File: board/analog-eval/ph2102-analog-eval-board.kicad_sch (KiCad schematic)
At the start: 41 parts, among them J1 CONN_PROBE, U1 LMC662, U2 TLV2333, U3 REF3020, U4 MCP3201-BI/SN, U5 LM27762

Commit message: 板子修改
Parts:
- removed U?: ESP32-PICO-D4, Package_DFN_QFN:QFN-48-1EP_7x7mm_P0.5mm_EP5.3x5.3mm, symbol RF_Module:ESP32-PICO-D4
- added R18: 0R0, Resistor_SMD:R_0805_2012Metric, symbol Device:R_Small
- R7: footprint (none) -> Resistor_SMD:R_0402_1005Metric
- U1: footprint (none) -> Package_SO:SOIC-8_3.9x4.9mm_P1.27mm
- gave numbers to parts that had none: 8
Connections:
- net at R10.1, R9.1, U1.3 (+): now also R18.1; no longer U1.6 (-)
- new net: R18.2, U1.6 (-)
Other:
- title: (none) -> PH 计模拟前端验证版
- moved on the sheet: C14, C15, C16, R13, R14, R15, R16, R17, U5

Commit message: update
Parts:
- removed NT1: NetTie_3_Tee, symbol Device:NetTie_3_Tee
- added C17: 10u, Capacitor_SMD:C_0603_1608Metric, symbol Device:C_Small
- added C18, C19: 2u2, Capacitor_SMD:C_0603_1608Metric, symbol Device:C_Small
- added C20, C21: 100n, Capacitor_SMD:C_0603_1608Metric, symbol Device:C_Small
- added C22: 100u, Capacitor_Tantalum_SMD:CP_EIA-3528-15_AVX-H, symbol Device:C_Polarized_Small
- added H1, H2, H3, H4: M3, MountingHole:MountingHole_3.2mm_M3_Pad_Via, symbol Mechanical:MountingHole_Pad
- added J2: CONN_OUT, Connector_PinHeader_2.54mm:PinHeader_1x10_P2.54mm_Vertical, symbol Connector_Generic:Conn_01x10
- added J3: CONN_NTC, Connector_JST:JST_XH_S2B-XH-A-1_1x02_P2.50mm_Horizontal, symbol Connector_Generic:Conn_01x02
- added NT1: NetTie_2, NetTie:NetTie-2_SMD_Pad2.0mm, symbol Device:NetTie_2
- added R19: 10k/1%, Resistor_SMD:R_0603_1608Metric, symbol Device:R_Small
- added R21, R22: 100R, Resistor_SMD:R_0603_1608Metric, symbol Device:R_Small
- added R23: 10k, Resistor_SMD:R_0603_1608Metric, symbol Device:R_Small
- added TP1: TP_PGOOD, TestPoint:TestPoint_Pad_D1.0mm, symbol Connector:TestPoint
- added TP2: TP_GUARD, symbol Connector:TestPoint
- added TP3: TP_+2V5, TestPoint:TestPoint_Pad_D1.0mm, symbol Connector:TestPoint
- added TP4: TP_-2V5, TestPoint:TestPoint_Pad_D1.0mm, symbol Connector:TestPoint
- C1, C10, C11, C12, C13, C14, C15, C2, C3, C4, C5, C6, C8, C9: footprint (none) -> Capacitor_SMD:C_0603_1608Metric
- C16: value 1u -> 4u7; footprint (none) -> Capacitor_SMD:C_0603_1608Metric
- C7: value 100n -> 1n; footprint (none) -> Capacitor_SMD:C_0603_1608Metric
- J1: footprint (none) -> Connector_Coaxial:BNC_Amphenol_B6252HB-NPP3G-50_Horizontal
- R1, R2, R3, R4: value 100k -> 10k/1%; footprint (none) -> Resistor_SMD:R_0603_1608Metric
- R10: value 91k -> 9.1k/1%; footprint (none) -> Resistor_SMD:R_0603_1608Metric
- R11, R12, R14, R15, R16, R17, R5, R6, R8: footprint (none) -> Resistor_SMD:R_0603_1608Metric
- R13: value R_Small -> 10k; footprint (none) -> Resistor_SMD:R_0603_1608Metric
- R18: footprint Resistor_SMD:R_0805_2012Metric -> Resistor_SMD:R_1206_3216Metric_Pad1.30x1.75mm_HandSolder
- R7: footprint Resistor_SMD:R_0402_1005Metric -> Resistor_SMD:R_0603_1608Metric
- R9: value 91k -> 10k/1%; footprint (none) -> Resistor_SMD:R_0603_1608Metric
- U2, U4: footprint (none) -> Package_SO:SOIC-8_3.9x4.9mm_P1.27mm
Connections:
- net +3V0 is gone; now on net +2V5: C4.2, C5.2, U3.1 (IN)
- net +2V5: now also R14.1, U5.11 (OUT+), C18.1, TP3.1
- net +3V3: now also U5.12 (EN+), U5.8 (EN-), C17.2, C22.1, J2.1 (Pin_1); no longer R13.2
- net -2V5: now also R15.2, U5.6 (OUT-), C19.2, TP4.1
- net ADC_CS: now also J2.3 (Pin_3)
- net ADC_MISO: now also J2.4 (Pin_4)
- net ADC_SCK: now also J2.5 (Pin_5)
- net GNDA: now also R16.2, R17.2, C17.1, C18.2, C19.1, C20.2, C21.2, C22.2, H1.1, H2.1, H3.1, H4.1, J2.10 (Pin_10), J2.6 (Pin_6), J3.2 (Pin_2), NT1.1
- net GUARD: now also TP2.1
- net VREF: now also J2.7 (Pin_7), R19.2
- net at C6.2, R12.2, R6.2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: now also R22.1; no longer C7.2, U4.2 (IN+)
- net at R13.1: now also TP1.1; no longer U5.1 (PGOOD)
- net at U2.5 (+): now also C21.1, R23.2
- net at U2.6 (-): now also U2.7, R21.1
- new net: R13.2, U5.1 (PGOOD)
- new net GND: J2.2 (Pin_2), NT1.2
- new net NTC_IN: J3.1 (Pin_1), R19.1, R23.1
- new net NTC_OUT: C20.1, J2.8 (Pin_8), R21.2
- new net VPH: C7.2, J2.9 (Pin_9), R22.2, U4.2 (IN+)
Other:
- moved on the sheet: C1, C10, C11, C12, C13, C14, C15, C16, C2, C3, C4, C5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

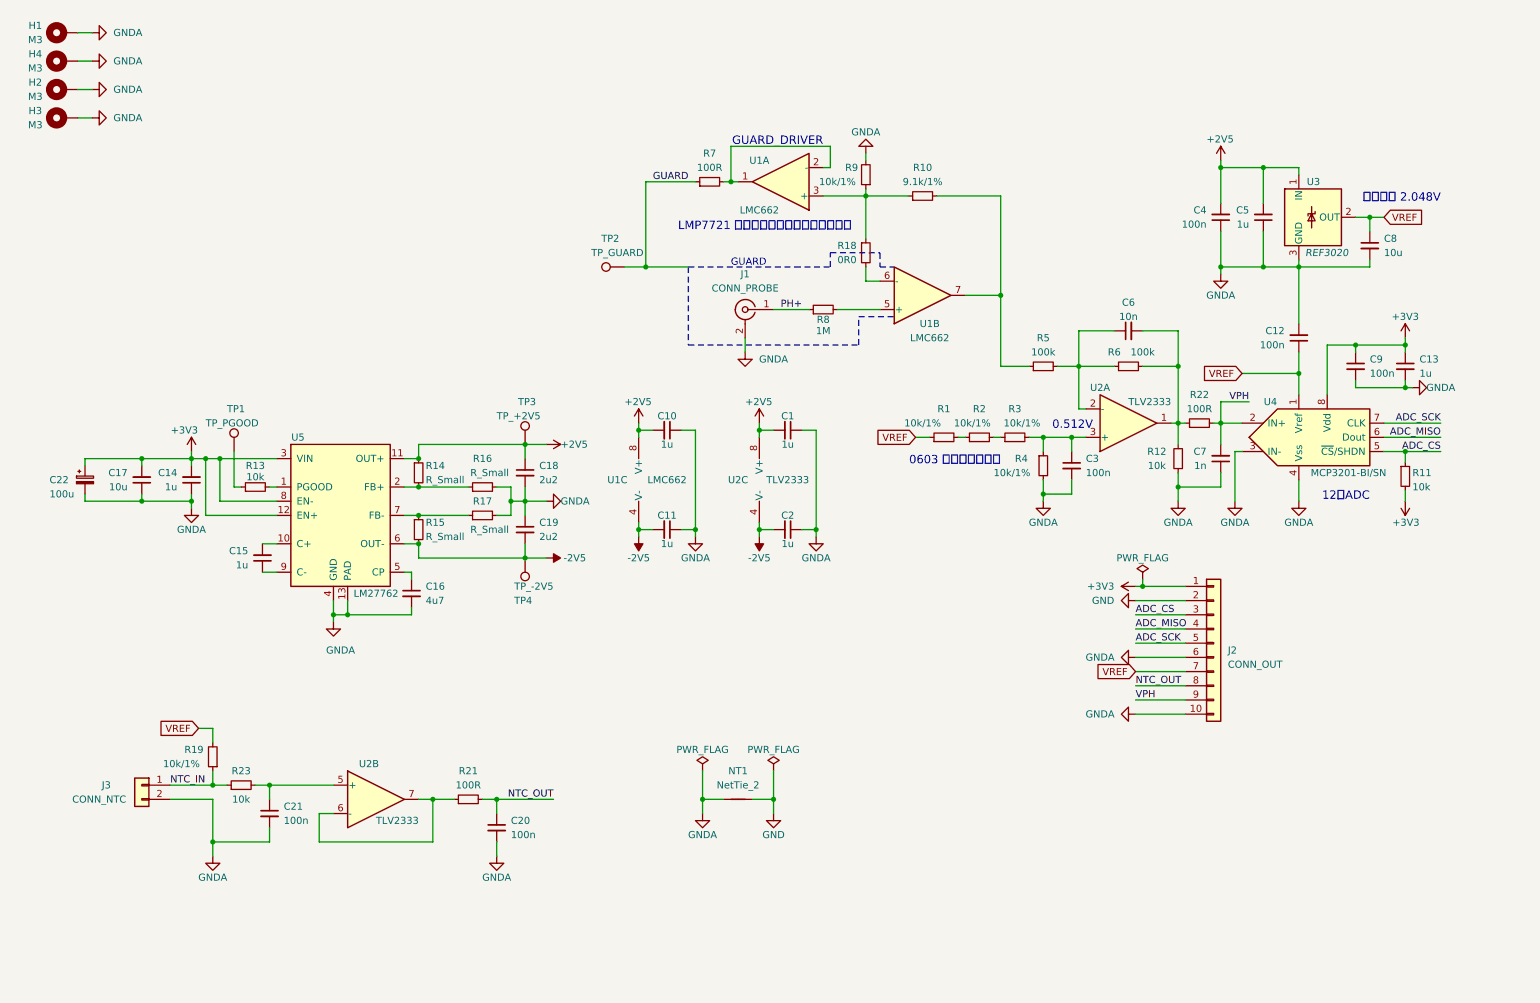
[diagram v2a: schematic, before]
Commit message: 完善 layout
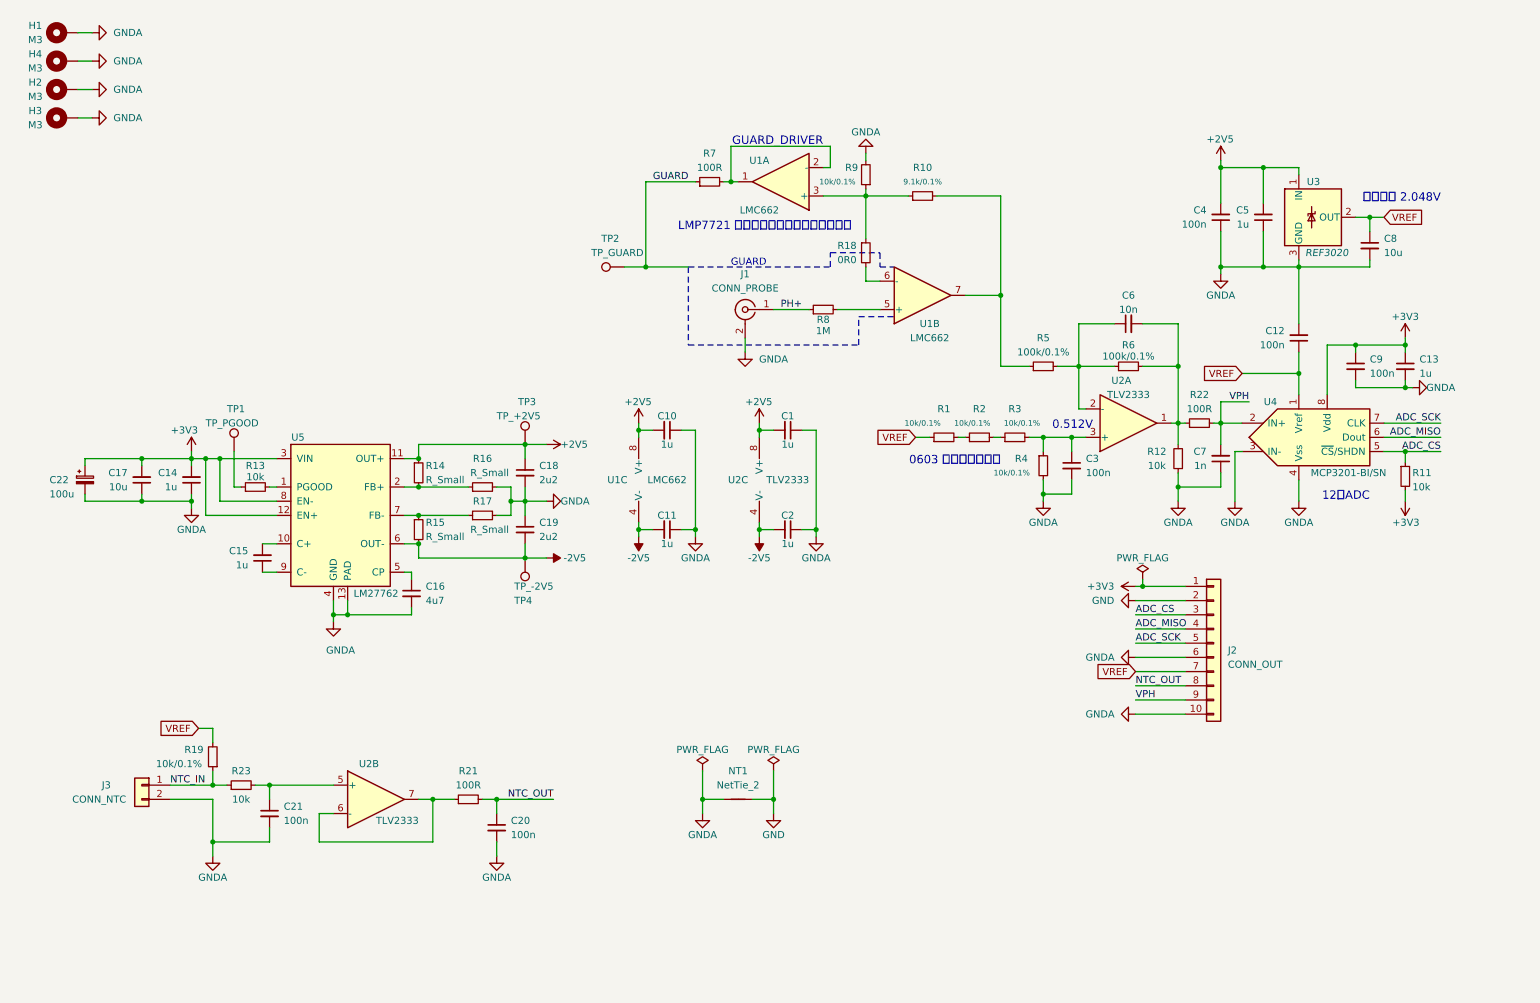
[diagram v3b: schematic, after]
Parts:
- R1, R19, R2, R3, R4, R9: value 10k/1% -> 10k/0.1%
- R10: value 9.1k/1% -> 9.1k/0.1%
- R5, R6: value 100k -> 100k/0.1%
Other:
- moved on the sheet: C6
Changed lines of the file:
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@@
     (stroke (width 0) (type solid) (color 0 0 0 0))
   )
-  (wire (pts (xy 203.2 69.85) (xy 203.2 76.2))
+  (wire (pts (xy 203.2 68.58) (xy 203.2 76.2))
     (stroke (width 0) (type solid) (color 0 0 0 0))
   )
@@
     (stroke (width 0) (type solid) (color 0 0 0 0))
   )
-  (wire (pts (xy 209.55 69.85) (xy 203.2 69.85))
+  (wire (pts (xy 209.55 68.58) (xy 203.2 68.58))
     (stroke (width 0) (type solid) (color 0 0 0 0))
   )
@@
     (stroke (width 0) (type solid) (color 0 0 0 0))
   )
-  (wire (pts (xy 214.63 69.85) (xy 220.98 69.85))
+  (wire (pts (xy 214.63 68.58) (xy 220.98 68.58))
     (stroke (width 0) (type solid) (color 0 0 0 0))
   )
@@
     (stroke (width 0) (type solid) (color 0 0 0 0))
   )
-  (wire (pts (xy 220.98 69.85) (xy 220.98 76.2))
+  (wire (pts (xy 220.98 68.58) (xy 220.98 76.2))
     (stroke (width 0) (type solid) (color 0 0 0 0))
   )
@@
       (effects (font (size 1.27 1.27)) (justify right))
     )
-    (property "Value" "10k/1%" (id 1) (at 39.37 147.32 0)
+    (property "Value" "10k/0.1%" (id 1) (at 38.1 147.32 0)
       (effects (font (size 1.27 1.27)) (justify right))
     )
@@
     (in_bom yes) (on_board yes)
     (property "Reference" "R9" (id 0) (at 162.56 40.64 0))
-    (property "Value" "10k/1%" (id 1) (at 160.02 43.18 0))
+    (property "Value" "10k/0.1%" (id 1) (at 160.02 43.18 0)
+      (effects (font (size 1 1)))
+    )
     (property "Footprint" "Resistor_SMD:R_0603_1608Metric" (id 2) (at 165.1 41.91 0)
       (effects (font (size 1.27 1.27)) hide)
@@
     (in_bom yes) (on_board yes)
     (property "Reference" "R10" (id 0) (at 175.26 40.64 90))
-    (property "Value" "9.1k/1%" (id 1) (at 175.26 43.18 90))
+    (property "Value" "9.1k/0.1%" (id 1) (at 175.26 43.18 90)
+      (effects (font (size 1 1)))
+    )
     (property "Footprint" "Resistor_SMD:R_0603_1608Metric" (id 2) (at 175.26 45.72 0)
       (effects (font (size 1.27 1.27)) hide)
@@
     (in_bom yes) (on_board yes)
     (property "Reference" "R1" (id 0) (at 179.07 83.82 90))
-    (property "Value" "10k/1%" (id 1) (at 175.26 86.36 90))
+    (property "Value" "10k/0.1%" (id 1) (at 175.26 86.36 90)
+      (effects (font (size 1 1)))
+    )
     (property "Footprint" "Resistor_SMD:R_0603_1608Metric" (id 2) (at 179.07 88.9 0)
       (effects (font (size 1.27 1.27)) hide)
@@
     (in_bom yes) (on_board yes)
     (property "Reference" "R2" (id 0) (at 185.42 83.82 90))
-    (property "Value" "10k/1%" (id 1) (at 184.15 86.36 90))
+    (property "Value" "10k/0.1%" (id 1) (at 184.15 86.36 90)
+      (effects (font (size 1 1)))
+    )
     (property "Footprint" "Resistor_SMD:R_0603_1608Metric" (id 2) (at 185.42 88.9 0)
       (effects (font (size 1.27 1.27)) hide)
@@
     (in_bom yes) (on_board yes)
     (property "Reference" "R3" (id 0) (at 191.77 83.82 90))
-    (property "Value" "10k/1%" (id 1) (at 193.04 86.36 90))
+    (property "Value" "10k/0.1%" (id 1) (at 193.04 86.36 90)
+      (effects (font (size 1 1)))
+    )
     (property "Footprint" "Resistor_SMD:R_0603_1608Metric" (id 2) (at 191.77 88.9 0)
       (effects (font (size 1.27 1.27)) hide)
@@
     (in_bom yes) (on_board yes)
     (property "Reference" "R5" (id 0) (at 196.85 71.12 90))
-    (property "Value" "100k" (id 1) (at 196.85 73.66 90))
+    (property "Value" "100k/0.1%" (id 1) (at 196.85 73.66 90))
     (property "Footprint" "Resistor_SMD:R_0603_1608Metric" (id 2) (at 196.85 76.2 0)
       (effects (font (size 1.27 1.27)) hide)
@@
       (effects (font (size 1.27 1.27)) (justify left))
     )
-    (property "Value" "10k/1%" (id 1) (at 187.96 95.25 0)
-      (effects (font (size 1.27 1.27)) (justify left))
+    (property "Value" "10k/0.1%" (id 1) (at 187.96 95.25 0)
+      (effects (font (size 1 1)) (justify left))
     )
     (property "Footprint" "Resistor_SMD:R_0603_1608Metric" (id 2) (at 196.85 93.98 0)
@@
   (symbol (lib_id "Device:R_Small") (at 212.09 76.2 90) (unit 1)
     (in_bom yes) (on_board yes)
-    (property "Reference" "R6" (id 0) (at 209.55 73.66 90))
-    (property "Value" "100k" (id 1) (at 214.63 73.66 90))
+    (property "Reference" "R6" (id 0) (at 212.09 72.39 90))
+    (property "Value" "100k/0.1%" (id 1) (at 212.09 73.66 90)
+      (effects (font (size 1.27 1.27)) (justify bottom))
+    )
     (property "Footprint" "Resistor_SMD:R_0603_1608Metric" (id 2) (at 212.09 76.2 0)
       (effects (font (size 1.27 1.27)) hide)
@@
     (pin "2")
   )
-  (symbol (lib_id "Device:C_Small") (at 212.09 69.85 90) (unit 1)
-    (in_bom yes) (on_board yes)
-    (property "Reference" "C6" (id 0) (at 212.09 64.77 90))
-    (property "Value" "10n" (id 1) (at 212.09 67.31 90))
-    (property "Footprint" "Capacitor_SMD:C_0603_1608Metric" (id 2) (at 212.09 69.85 0)
-      (effects (font (size 1.27 1.27)) hide)
-    )
-    (property "Datasheet" "~" (id 3) (at 212.09 69.85 0)
+  (symbol (lib_id "Device:C_Small") (at 212.09 68.58 90) (unit 1)
+    (in_bom yes) (on_board yes)
+    (property "Reference" "C6" (id 0) (at 212.09 63.5 90))
+    (property "Value" "10n" (id 1) (at 212.09 66.04 90))
+    (property "Footprint" "Capacitor_SMD:C_0603_1608Metric" (id 2) (at 212.09 68.58 0)
+      (effects (font (size 1.27 1.27)) hide)
+    )
+    (property "Datasheet" "~" (id 3) (at 212.09 68.58 0)
       (effects (font (size 1.27 1.27)) hide)
     )
@@
   (symbol (lib_id "Amplifier_Operational:MCP6002-xSN") (at 212.09 86.36 0) (mirror x) (unit 1)
     (in_bom yes) (on_board yes)
-    (property "Reference" "U2" (id 0) (at 207.01 80.01 0))
-    (property "Value" "TLV2333" (id 1) (at 215.9 82.55 0))
+    (property "Reference" "U2" (id 0) (at 210.82 78.74 0))
+    (property "Value" "TLV2333" (id 1) (at 212.09 81.28 0))
     (property "Footprint" "Package_SO:SOIC-8_3.9x4.9mm_P1.27mm" (id 2) (at 212.09 86.36 0)
       (effects (font (size 1.27 1.27)) hide)
@@
     )
     (path "/aad8282b-738f-4501-ab85-a0e4570e620f"
-      (reference "R1") (unit 1) (value "10k/1%") (footprint "Resistor_SMD:R_0603_1608Metric")
+      (reference "R1") (unit 1) (value "10k/0.1%") (footprint "Resistor_SMD:R_0603_1608Metric")
     )
     (path "/7c521a9e-00d3-4834-975e-9315d38c98bd"
-      (reference "R2") (unit 1) (value "10k/1%") (footprint "Resistor_SMD:R_0603_1608Metric")
+      (reference "R2") (unit 1) (value "10k/0.1%") (footprint "Resistor_SMD:R_0603_1608Metric")
     )
     (path "/cc9a56c9-3186-4b00-a7a7-e8fe0d49fb75"
-      (reference "R3") (unit 1) (value "10k/1%") (footprint "Resistor_SMD:R_0603_1608Metric")
+      (reference "R3") (unit 1) (value "10k/0.1%") (footprint "Resistor_SMD:R_0603_1608Metric")
     )
     (path "/126014eb-ea26-4314-bd8e-f8dee9a57889"
-      (reference "R4") (unit 1) (value "10k/1%") (footprint "Resistor_SMD:R_0603_1608Metric")
+      (reference "R4") (unit 1) (value "10k/0.1%") (footprint "Resistor_SMD:R_0603_1608Metric")
     )
     (path "/e779bf39-5e18-43c3-a404-9bbfdda7f81b"
-      (reference "R5") (unit 1) (value "100k") (footprint "Resistor_SMD:R_0603_1608Metric")
+      (reference "R5") (unit 1) (value "100k/0.1%") (footprint "Resistor_SMD:R_0603_1608Metric")
     )
     (path "/d8210768-d0c3-4c82-a0af-8d04b1fbda46"
-      (reference "R6") (unit 1) (value "100k") (footprint "Resistor_SMD:R_0603_1608Metric")
+      (reference "R6") (unit 1) (value "100k/0.1%") (footprint "Resistor_SMD:R_0603_1608Metric")
     )
     (path "/bdf6476a-f1db-476a-a18d-a8d1e8052211"
@@
     )
     (path "/3f39c93c-c2c7-4bf6-8100-26652e48dc6f"
-      (reference "R9") (unit 1) (value "10k/1%") (footprint "Resistor_SMD:R_0603_1608Metric")
+      (reference "R9") (unit 1) (value "10k/0.1%") (footprint "Resistor_SMD:R_0603_1608Metric")
     )
     (path "/5580d341-143e-4dac-bcc5-52bc74144206"
-      (reference "R10") (unit 1) (value "9.1k/1%") (footprint "Resistor_SMD:R_0603_1608Metric")
+      (reference "R10") (unit 1) (value "9.1k/0.1%") (footprint "Resistor_SMD:R_0603_1608Metric")
     )
     (path "/fc60e513-3af1-4244-b8f8-adeeb2f48218"
@@
     )
     (path "/338a0a46-3a7f-493a-83ac-76ba361aec6e"
-      (reference "R19") (unit 1) (value "10k/1%") (footprint "Resistor_SMD:R_0603_1608Metric")
+      (reference "R19") (unit 1) (value "10k/0.1%") (footprint "Resistor_SMD:R_0603_1608Metric")
     )
     (path "/485e51e6-c5d1-45c4-94db-6b071a98798d"

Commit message: ready to fabricate
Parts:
- removed TP3: TP_+2V5, TestPoint:TestPoint_Pad_D1.0mm, symbol Connector:TestPoint
- removed TP4: TP_-2V5, TestPoint:TestPoint_Pad_D1.0mm, symbol Connector:TestPoint
- added TP3: TP_2V5, Connector_PinHeader_2.54mm:PinHeader_1x02_P2.54mm_Vertical, symbol Connector:TestPoint_2Pole
- R14, R15: value R_Small -> 76.8k
- R16, R17: value R_Small -> 73.2k
- R5, R6: value 100k/0.1% -> 10k/0.1%
- R8: value 1M -> 1M/1%
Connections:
- net +2V5: now also TP3.1
- net -2V5: now also TP3.2
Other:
- note added: "VOUT = 1.2V × (R1 + R2) / R2"
- note removed: "0603 电阻都用低温漂"
- company: (none) -> Rednecks Engineering Labs.
- title: PH 计模拟前端验证版 -> ph Meter Eval Board

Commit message: add firmware
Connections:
- net NTC_OUT: now also J2.9 (Pin_9); no longer J2.8 (Pin_8)
- net VPH: now also J2.8 (Pin_8); no longer J2.9 (Pin_9)
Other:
- note removed: "LMP7721 同向输入端加保护环防止漏电流"
- moved on the sheet: TP2
